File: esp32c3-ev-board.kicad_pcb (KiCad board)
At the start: 2 copper layers, 59 parts, among them IC1 ESP32-C3FH4, IC2 W25Q128JVSIQ, IC3 ACS711EEXTK-31AB-T, IC4 SPX3819M5-L-3-3, J2 Barrel_Jack, J3 USB_C_Receptacle_USB2.0, J4 Conn_01x04_Pin, SW2 SW_DPST_x2, SW3 SW_DPST_x2, U1 USBLC6-2SC6, U3 USBLC6-2SC6, Y1 40MHZ

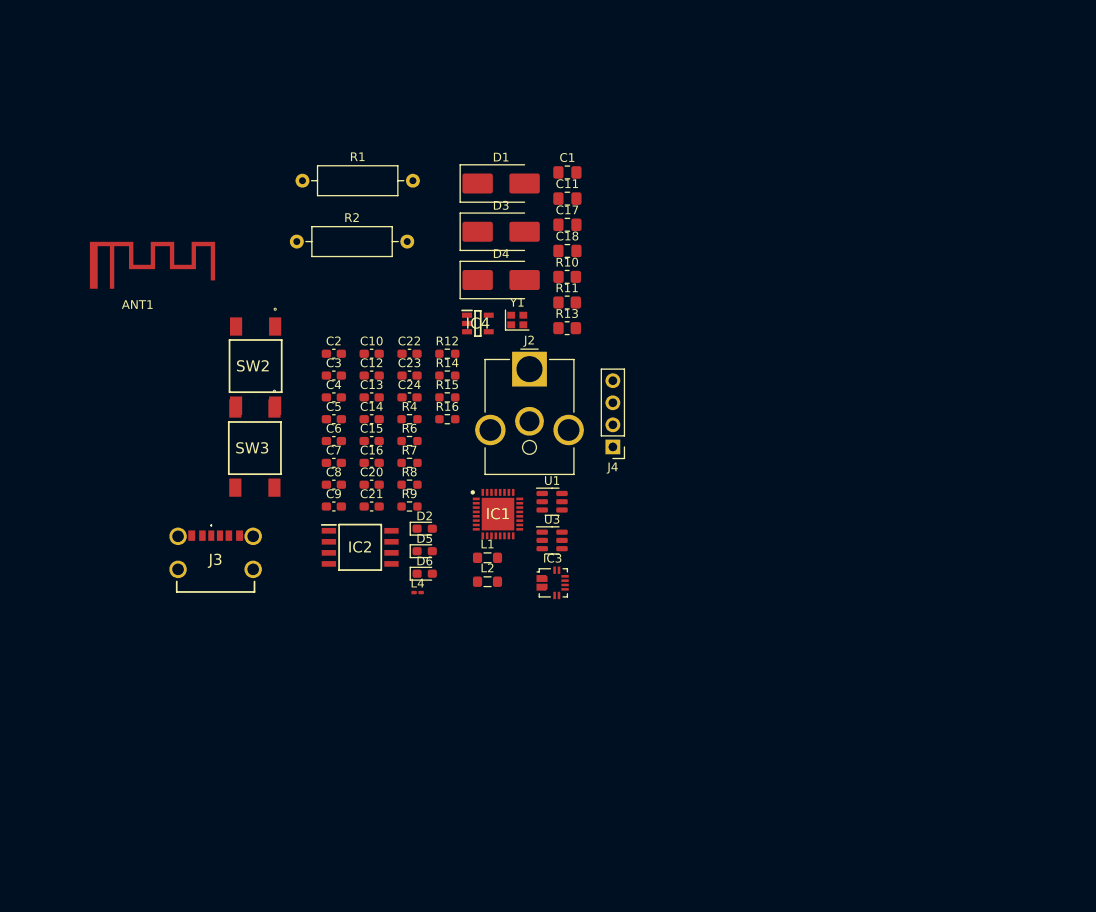
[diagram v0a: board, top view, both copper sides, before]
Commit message: Arranged some of the components for less crosses in the pcb
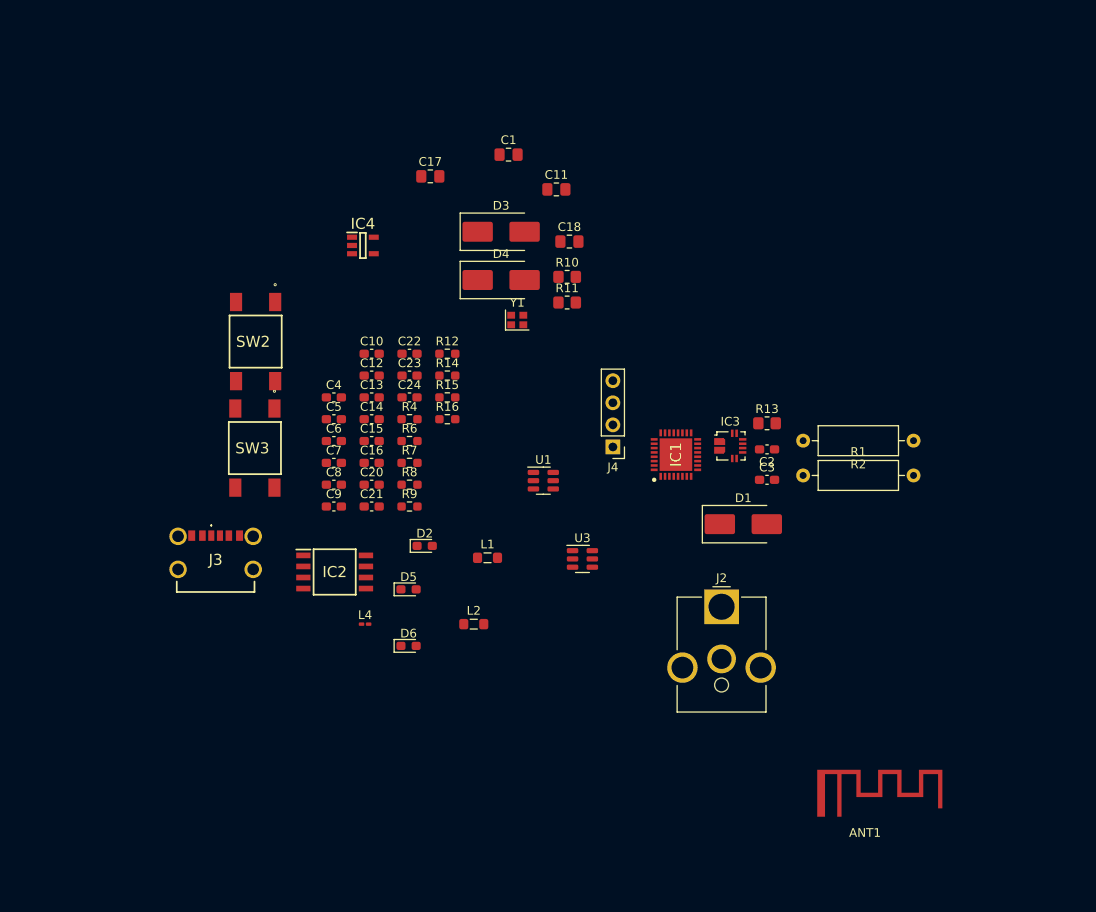
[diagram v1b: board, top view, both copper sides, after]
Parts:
- moved ANT1 103.4 mm to (201.5, 148.0)
- moved R2 74.5 mm to (207.1, 102.4), turned to 180 degrees
- moved R1 66.8 mm to (194.4, 106.4)
- moved C3 51.2 mm to (190.2, 106.9)
- moved C2 51.0 mm to (190.2, 103.4), turned to 180 degrees
- moved D1 48.1 mm to (187.5, 112.0)
- moved J2 35.1 mm to (185.0, 121.5)
- moved IC3 25.8 mm to (186.0, 103.0)
- moved R13 25.5 mm to (190.2, 100.4)
- moved IC1 21.6 mm to (179.8, 104.0), turned to 90 degrees
- moved C17 16.7 mm to (151.5, 72.0)
- moved IC4 16.0 mm to (143.8, 80.0)
- moved D6 8.50 mm to (149.0, 126.0)
- moved C1 7.07 mm to (160.5, 69.5)
- moved L4 7.05 mm to (144.0, 123.5)
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
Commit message: Did some pcb changes
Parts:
- moved C8 56.6 mm to (196.5, 115.0)
- moved R12 56.2 mm to (200.3, 123.5), turned to 180 degrees
- moved J3 55.5 mm to (178.8, 135.9)
- moved C15 54.5 mm to (196.0, 121.0), turned to 180 degrees
- moved C4 52.9 mm to (186.8, 123.0)
- moved C5 52.8 mm to (186.6, 125.5)
- moved R6 51.2 mm to (195.8, 123.5)
- moved IC2 49.0 mm to (189.0, 110.5), turned to 180 degrees
- moved D2 46.8 mm to (195.0, 99.0)
- moved SW2 46.7 mm to (164.0, 124.5)
- moved C10 46.1 mm to (184.6, 115.5)
- moved SW3 45.4 mm to (171.5, 124.5)
- moved R10 44.4 mm to (182.0, 125.5), turned to 180 degrees
- moved L2 43.7 mm to (200.2, 121.0)
- moved C17 43.3 mm to (185.0, 99.5)
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
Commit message: Changed footprints
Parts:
- L4: footprint Inductor_SMD:L_0201_0603Metric_Pad0.64x0.40mm_HandSolder -> Inductor_SMD:L_0603_1608Metric_Pad1.05x0.95mm_HandSolder
- R12, R16, R4, R6, R7, R8, R9: footprint Resistor_SMD:R_0603_1608Metric_Pad0.98x0.95mm_HandSolder -> Resistor_SMD:R_1206_3216Metric_Pad1.30x1.75mm_HandSolder
- moved R9 0.76 mm to (182.5, 129.5)

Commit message: Assigned new switch and DC connecter footprints
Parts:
- J2: value Barrel_Jack -> DC Connecter; footprint Connector_BarrelJack:BarrelJack_CUI_PJ-063AH_Horizontal_CircularHoles -> KLDX-0202-A:KLDX0202A
- SW2, SW3: footprint FSM2JSMAATR:FSM2J_1 -> SKRPANE010:SKRPADE010
- moved J2 9.23 mm to (199.2, 85.3)

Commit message: placement and routing ideas
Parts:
- removed the R4 at (173.1, 109.0)
- added H1: MountingHole_Pad, MountingHole:MountingHole_2.7mm_M2.5_Pad, F.Cu at (223.4, 58.5)
- added H2: MountingHole_Pad, MountingHole:MountingHole_2.7mm_M2.5_Pad, F.Cu at (223.4, 68.6)
- added H3: MountingHole_Pad, MountingHole:MountingHole_2.7mm_M2.5_Pad, F.Cu at (223.4, 78.8)
- added H4: MountingHole_Pad, MountingHole:MountingHole_2.7mm_M2.5_Pad, F.Cu at (223.4, 88.9)
- added R12: 22R, Resistor_SMD:R_1206_3216Metric_Pad1.30x1.75mm_HandSolder, F.Cu at (124.5, 103.5)
- J5: renamed from J3; footprint USB4125-GF-A-0190:USB4125GFA0190 -> Connector_USB:USB_C_Receptacle_GCT_USB4105-xx-A_16P_TopMnt_Horizontal
- moved J4 97.2 mm to (105.4, 78.2), turned to 0 degrees
- moved J5 90.3 mm to (127.6, 61.5), turned to 180 degrees
- moved R13 90.0 mm to (121.0, 63.8), turned to 90 degrees
- moved SW3 86.7 mm to (113.4, 60.2)
- moved R4 83.2 mm to (140.8, 65.3), turned to 0 degrees
- moved R14 78.6 mm to (134.3, 63.8), turned to -90 degrees
- moved R5 75.0 mm to (115.7, 65.2), turned to 180 degrees
- moved C18 74.7 mm to (110.8, 65.2), turned to 180 degrees
- moved U2 72.4 mm to (116.0, 85.6), turned to 90 degrees
- moved SW2 66.9 mm to (143.6, 60.8)
- moved L2 66.2 mm to (134.5, 112.1), turned to 90 degrees
- moved U1 61.8 mm to (127.2, 70.9), turned to 90 degrees
- moved C12 61.0 mm to (135.3, 115.2), turned to 0 degrees
- moved L3 60.4 mm to (131.7, 112.1), turned to 90 degrees
- moved Y1 59.9 mm to (117.0, 102.5), turned to 90 degrees
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- renumbered C2 to C1, C13 to C10, C14 to C11, C15 to C12, C16 to C13, C17 to C14, C4 to C15, C5 to C16, C20 to C17, C24 to C18, C10 to C19, C21 to C2, C8 to C20, C6 to C21, C7 to C22, C9 to C3, C18 to C4, C22 to C5, C1 to C6, C3 to C7, C11 to C8, C12 to C9, D2 to D1, D1 to D2, D5 to D3, D3 to D5, IC4 to IC1, IC3 to IC2, IC1 to IC3, IC2 to IC4, L4 to L1, L1 to L3, R13 to R1, R14 to R10, R15 to R11, R9 to R13, R8 to R14, R1 to R2, R2 to R3, R12 to R4, R16 to R5, R11 to R6, R6 to R8, R10 to R9, U3 to U2
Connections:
- ANT1 pad 1: GND -> Reg Neg
- C1 pad 1: GND -> Reg Neg
- C10 pad 2: GND -> Reg Neg
- C11 pad 2: GND -> Reg Neg
- C12 pad 2: GND -> Reg Neg
- C13 pad 2: GND -> Reg Neg
- C14 pad 2: GND -> Reg Neg
- C15 pad 2: GND -> Reg Neg
- C16 pad 2: GND -> Reg Neg
- C17 pad 2: GND -> Reg Neg
- C18 pad 2: GND -> Reg Neg
- C19 pad 2: GND -> Reg Neg
- C20 pad 2: GND -> Reg Neg
- C21 pad 2: GND -> Reg Neg
- C22 pad 2: GND -> Reg Neg
- C23 pad 2: GND -> Reg Neg
- C6 pad 2: GND -> Reg Neg
- C7 pad 2: GND -> Reg Neg
- C8 pad 2: GND -> Reg Neg
- C9 pad 2: GND -> Reg Neg
- IC2 pad 4: UnregNeg(closest to bat term) -> Reg Neg
- IC2 pad 5: GND -> Reg Neg
- IC3 pad 33: GND -> Reg Neg
- IC4 pad 4: GND -> Reg Neg
- J4 pad 3: GND -> Reg Neg
- J5 pad A12: Net-(J3-GND-PadA12) -> (no net)
- J5 pad A9: GND -> 5vUSB
- J5 pad B12: Net-(J3-GND-PadA12) -> (no net)
- J5 pad B9: GND -> 5vUSB
- R13 pad 1: GND -> Reg Neg
- R14 pad 2: GND -> Reg Neg
- R3 pad 2: GND -> Reg Neg
- R6 pad 1: GND -> Reg Neg
- R9 pad 1: GND -> Reg Neg
- U1 pad 2: GND -> Reg Neg
- U1 pad 4: Net-(J3-D--PadA7) -> Net-(J5-D--PadA7)
- U1 pad 6: Net-(J3-D+-PadA6) -> Net-(J5-D+-PadA6)
- U2 pad 2: GND -> Reg Neg
- Y1 pad 2: GND -> Reg Neg
- Y1 pad 4: GND -> Reg Neg
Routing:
- net Net-(IC3-XTAL_N): track 0.00 -> 16.9 mm
- net Net-(D4-A): track 0.00 -> 12.6 mm
- net 5vUSB: track 0.00 -> 12.6 mm
- net CHIPEN: track 0.00 -> 9.69 mm
- net CurMeas: track 0.00 -> 9.26 mm
- net Net-(C21-Pad1): track 0.00 -> 8.43 mm
- net Net-(IC3-XTAL_P): track 0.00 -> 7.19 mm
- net Net-(J5-CC1): track 0.00 -> 7.18 mm
- net Net-(J5-CC2): track 0.00 -> 6.72 mm
- net Reg Pos: track 0.00 -> 6.08 mm
- net +3.3V: track 0.00 -> 2.98 mm
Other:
- copper layers 2 -> 4

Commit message: shape and placement nearly finished, doing perephirals next
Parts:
- added R15: 1k, Resistor_SMD:R_0805_2012Metric_Pad1.20x1.40mm_HandSolder, F.Cu at (154.1, 69.1)
- moved H2 111.5 mm to (112.2, 60.7)
- moved ANT1 70.5 mm to (125.7, 116.2), turned to 180 degrees
- moved H1 68.1 mm to (155.4, 60.4)
- moved D1 55.3 mm to (148.7, 68.8)
- moved C6 42.9 mm to (154.9, 74.8), turned to -90 degrees
- moved C5 35.4 mm to (151.5, 77.5), turned to 180 degrees
- moved R6 33.3 mm to (150.5, 111.7)
- moved R9 33.1 mm to (150.5, 115.3)
- moved D6 33.1 mm to (145.8, 114.9), turned to 180 degrees
- moved R8 27.8 mm to (167.9, 123.3)
- moved R7 23.5 mm to (183.1, 132.3)
- moved D3 13.7 mm to (146.0, 111.8), turned to 180 degrees
- moved J4 8.68 mm to (110.9, 71.5)
- moved SW3 6.70 mm to (120.1, 60.1)
- moved J2 6.27 mm to (141.2, 88.2)
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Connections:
- D1 pad 2: +3.3V -> Net-(D1-A)
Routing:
- net Net-(IC1-EN): track 0.00 -> 11.3 mm
- net Reg Pos: track 6.08 -> 9.85 mm
- net +3.3V: track 2.98 -> 5.52 mm
- net 5vUSB: track 12.6 -> 15.1 mm
- net Net-(IC1-ADJ/BYP): track 0.00 -> 1.82 mm

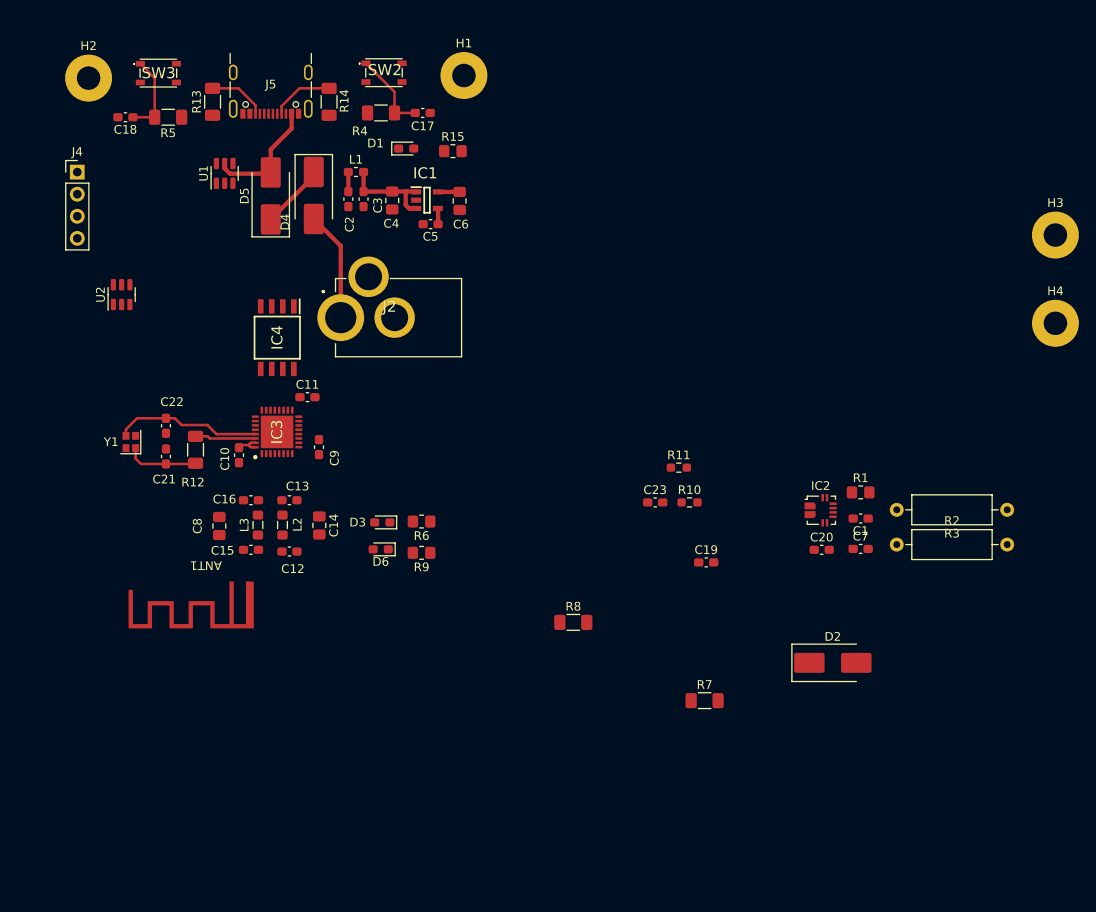
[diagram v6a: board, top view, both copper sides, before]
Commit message: almost completed board layout
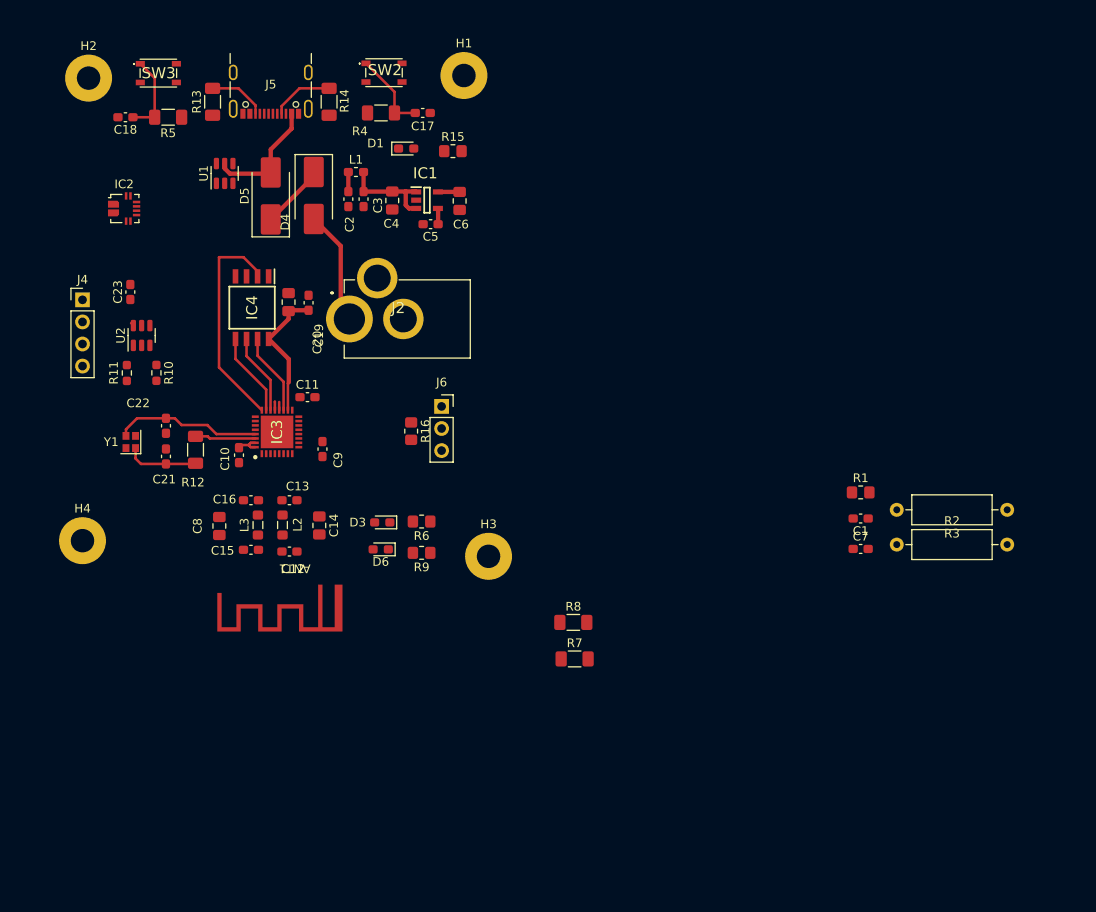
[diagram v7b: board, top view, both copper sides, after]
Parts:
- removed D2: D, Diode_SMD:D_SMB_Handsoldering
- added J6: Screw_Terminal_01x03, Connector_PinSocket_2.54mm:PinSocket_1x03_P2.54mm_Vertical, F.Cu at (152.8, 98.5)
- added R16: 1k, Resistor_SMD:R_0805_2012Metric_Pad1.20x1.40mm_HandSolder, F.Cu at (149.3, 101.3)
- C20: footprint Capacitor_SMD:C_0603_1608Metric_Pad1.08x0.95mm_HandSolder -> Capacitor_SMD:C_0805_2012Metric_Pad1.18x1.45mm_HandSolder
- moved H4 114.7 mm to (111.5, 113.9)
- moved IC2 87.3 mm to (116.3, 75.7)
- moved H3 74.9 mm to (158.2, 115.7)
- moved C20 67.6 mm to (135.2, 86.5), turned to 90 degrees
- moved C23 65.0 mm to (117.0, 85.3), turned to 90 degrees
- moved R11 64.4 mm to (116.6, 94.6), turned to -90 degrees
- moved R10 63.1 mm to (120.0, 94.6), turned to -90 degrees
- moved C19 54.6 mm to (137.5, 86.5), turned to 90 degrees
- moved R7 15.7 mm to (168.1, 127.5)
- moved J4 14.7 mm to (111.5, 86.2)
- moved ANT1 10.2 mm to (135.9, 116.6)
- moved U2 5.23 mm to (118.3, 90.3)
- moved IC4 4.51 mm to (131.0, 87.1)
- moved J2 1.01 mm to (142.2, 88.4)
- moved C9 0.46 mm to (139.1, 103.4)
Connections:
- IC3 pad 10: unconnected-(IC3-MTDI-Pad10) -> Net-(IC3-MTDI)
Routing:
- net Net-(IC3-SPIQ): track 0.00 -> 25.3 mm
- net Net-(IC3-VDD_SPI): track 0.00 -> 15.7 mm
- net Net-(IC3-SPID): track 0.00 -> 9.66 mm
- net Net-(IC3-SPICLK): track 0.00 -> 9.50 mm
- net Net-(IC3-SPIHD): track 0.00 -> 9.43 mm
- net Net-(IC3-SPICS0): track 0.00 -> 0.97 mm
- net Net-(IC3-SPIWP): track 0.00 -> 0.94 mm

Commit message: starting outline REMEMBER TO ORDER 100k resistor size 0805
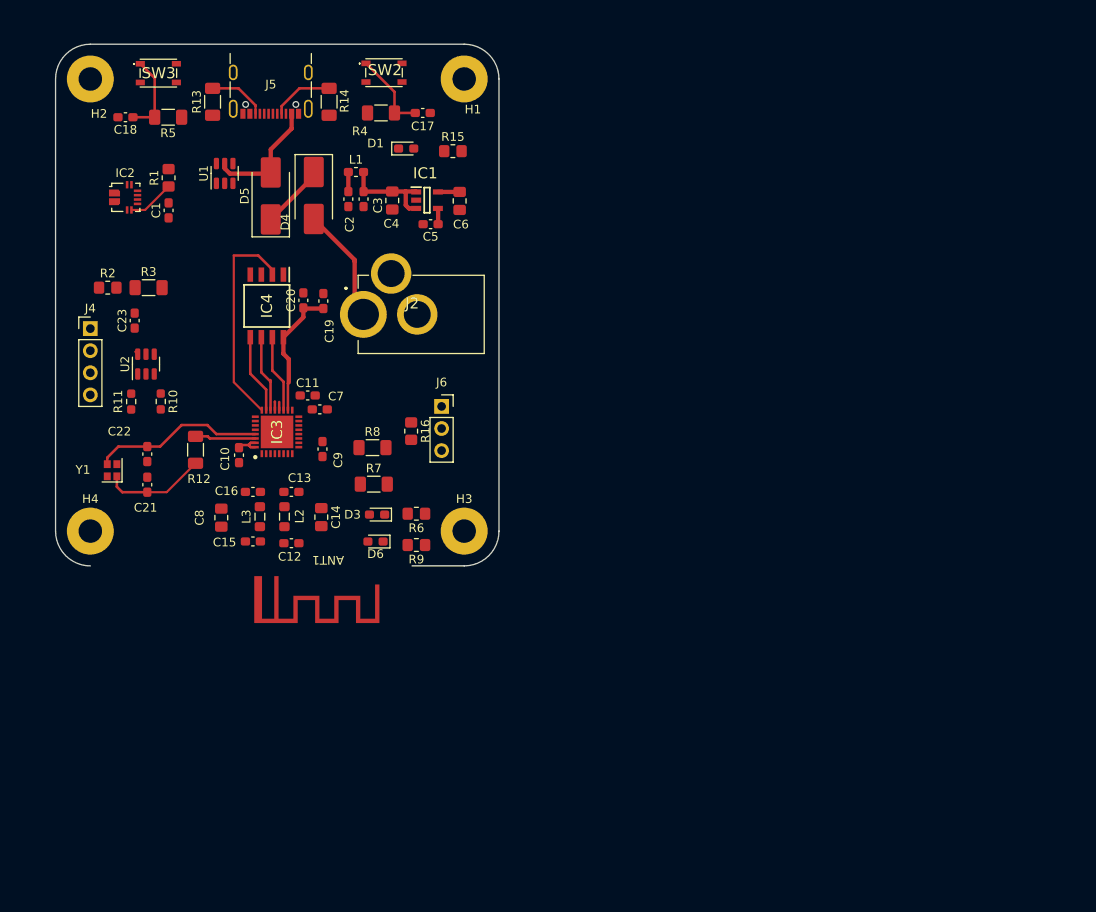
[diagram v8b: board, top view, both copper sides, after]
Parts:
- C19: value C -> 100n
- C20: value C -> 10u; footprint Capacitor_SMD:C_0805_2012Metric_Pad1.18x1.45mm_HandSolder -> Capacitor_SMD:C_0603_1608Metric_Pad1.08x0.95mm_HandSolder
- R2: value 180kR -> 100k; footprint Resistor_THT:R_Axial_DIN0309_L9.0mm_D3.2mm_P12.70mm_Horizontal -> Resistor_SMD:R_0805_2012Metric_Pad1.20x1.40mm_HandSolder
- R3: value 10kR -> 5.1k; footprint Resistor_THT:R_Axial_DIN0309_L9.0mm_D3.2mm_P12.70mm_Horizontal -> Resistor_SMD:R_1206_3216Metric_Pad1.30x1.75mm_HandSolder
- moved R3 102.0 mm to (119.1, 84.8), turned to 0 degrees
- moved R2 95.4 mm to (114.4, 84.8)
- moved R1 87.4 mm to (121.4, 72.2), turned to 90 degrees
- moved C1 87.1 mm to (121.4, 75.9), turned to 90 degrees
- moved C7 64.2 mm to (138.8, 98.8)
- moved R7 30.6 mm to (145.0, 107.4)
- moved R8 30.6 mm to (144.8, 103.2)
- moved H3 4.03 mm to (155.4, 112.8)
- moved ANT1 3.97 mm to (139.8, 115.6)
- moved C21 3.90 mm to (119.0, 107.5)
- moved C22 3.90 mm to (119.0, 103.9)
- moved Y1 3.90 mm to (114.9, 105.8)
- moved J4 3.43 mm to (112.4, 89.5)
- moved C23 3.33 mm to (117.5, 88.6)
- moved R10 3.33 mm to (120.5, 97.9)
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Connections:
- C7 pad 1: Net-(C7-Pad1) -> VoltMeas
- R2 pad 2: Net-(C7-Pad1) -> VoltMeas
- R3 pad 1: Net-(C7-Pad1) -> VoltMeas
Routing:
- net Net-(IC2-~{FAULT}): track 0.00 -> 5.39 mm
- net Net-(C21-Pad1): track 8.43 -> 12.1 mm
- net Net-(IC3-XTAL_N): track 16.9 -> 19.8 mm
- net Net-(IC3-SPIHD): track 9.43 -> 8.93 mm
- net Net-(IC3-SPID): track 9.66 -> 9.15 mm
- net Net-(IC3-VDD_SPI): track 15.7 -> 15.2 mm
- net Net-(IC3-SPIQ): track 25.3 -> 24.8 mm
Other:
- board outline added: 51 x 60 mm
